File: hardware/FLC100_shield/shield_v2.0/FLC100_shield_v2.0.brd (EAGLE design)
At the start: 99.1 x 78.7 mm, 68 parts, among them IC1 TSR 1-2450, IC4 MCP1640, J1 RJ11-6PTH, Q1 2N7000, Q2 2N7000, Q3 2N7000, Q4 2N7000, Q5 2N7000, Q6 2N7000, Q7 2N7000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

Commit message: Minor routing changes.
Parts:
- JP9: value CLOUD PWR -> CLOUD CTRL
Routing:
- net 6: track 38.6 -> 40.1 mm
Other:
- board text added: "Add diodes to select highest voltage between IOREF and +5V"
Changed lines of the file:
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@@
 <text x="-10.16" y="40.64" size="1.27" layer="26" ratio="10" rot="MR90">&gt;DRAWING_NAME</text>
 <text x="-5.08" y="38.1" size="1.27" layer="26" ratio="10" rot="MR90">&gt;PLOT_DATE_TIME</text>
-<text x="96.52" y="15.24" size="1.9304" layer="26" ratio="12" rot="MR0">FLC100 shield v1.0</text>
-<text x="96.52" y="17.78" size="1.016" layer="26" ratio="10" rot="MR0">http://github.com/stevemarple/FLC100_shield</text>
+<text x="96.52" y="15.24" size="1.9304" layer="122" ratio="12" rot="MR0">FLC100 shield v1.0</text>
+<text x="96.52" y="17.78" size="1.016" layer="122" ratio="10" rot="MR0">http://github.com/stevemarple/FLC100_shield</text>
 <wire x1="99.06" y1="77.47" x2="97.79" y2="78.74" width="0" layer="20" curve="90"/>
 <wire x1="1.27" y1="78.74" x2="0" y2="77.47" width="0" layer="20" curve="90"/>
@@
 <text x="1.27" y="75.565" size="1.27" layer="27" ratio="10">+3V3</text>
 <text x="14.605" y="76.835" size="1.016" layer="27" ratio="10">VIN</text>
-<text x="72.39" y="47.625" size="1.4224" layer="121" ratio="12" rot="R90">FLC100 shield v1.0</text>
+<text x="91.694" y="49.53" size="1.4224" layer="121" ratio="12" rot="R90">FLC100 shield v1.0</text>
 <wire x1="69.215" y1="10.795" x2="60.96" y2="10.795" width="0.254" layer="121"/>
 <wire x1="60.96" y1="10.795" x2="59.69" y2="9.525" width="0.254" layer="121"/>
@@
 <wire x1="60.325" y1="9.779" x2="59.69" y2="9.525" width="0.254" layer="121"/>
 <wire x1="53.34" y1="25.4" x2="99.06" y2="25.4" width="0.254" layer="122" style="longdash"/>
+<text x="32.385" y="40.005" size="1.524" layer="121" ratio="12">FLC100 shield v1.0</text>
+<text x="74.93" y="13.97" size="1.524" layer="121" ratio="12">FLC100 shield v1.0</text>
+<text x="-7.62" y="16.51" size="1.778" layer="122">Add diodes to select highest voltage
+between IOREF and +5V</text>
 </plain>
 <attributes>
@@
 <attribute name="VALUE" x="11.43" y="38.735" size="1.016" layer="27" ratio="10"/>
 </element>
-<element name="JP9" library="SparkFun" package="1X02" value="CLOUD PWR" x="83.82" y="33.02" smashed="yes">
-<attribute name="NAME" x="82.4738" y="34.8488" size="1.27" layer="25" ratio="10"/>
-<attribute name="VALUE" x="82.55" y="29.845" size="1.27" layer="27" ratio="10"/>
+<element name="JP9" library="SparkFun" package="1X02" value="CLOUD CTRL" x="83.82" y="33.02" smashed="yes">
+<attribute name="NAME" x="89.6112" y="30.4038" size="1.27" layer="25" ratio="10" rot="R90"/>
+<attribute name="VALUE" x="91.44" y="30.48" size="1.27" layer="27" ratio="10" rot="R90"/>
 </element>
 <element name="JP11" library="pinhead" package="2X03" value="ALT ISP" x="31.75" y="71.12" smashed="yes" rot="R180">
@@
 </element>
 <element name="XRF" library="SteveMarple" package="XBEE" value="" x="74.295" y="13.335" smashed="yes" rot="R270">
-<attribute name="NAME" x="97.79" y="11.43" size="1.27" layer="25" ratio="10" rot="R90"/>
+<attribute name="NAME" x="90.17" y="20.955" size="1.27" layer="25" ratio="10"/>
 <attribute name="VALUE" x="75.565" y="22.225" size="0.4064" layer="27" rot="R270"/>
 </element>
@@
 <element name="C2" library="SparkFun" package="CPOL-RADIAL-10UF-25V" value="4u7 25V" x="45.72" y="36.83" smashed="yes" rot="R270">
 <attribute name="NAME" x="48.26" y="32.385" size="1.27" layer="25" ratio="10" rot="R90"/>
-<attribute name="VALUE" x="49.911" y="32.385" size="1.27" layer="27" ratio="10" rot="R90"/>
+<attribute name="VALUE" x="49.911" y="31.115" size="1.27" layer="27" ratio="10" rot="R90"/>
 </element>
 <element name="U$5" library="SteveMarple" package="PAD" value="PAD" x="91.44" y="43.18" smashed="yes"/>
@@
 <wire x1="51.308" y1="73.152" x2="48.26" y2="76.2" width="0.254" layer="16"/>
 <wire x1="72.898" y1="73.152" x2="51.308" y2="73.152" width="0.254" layer="16"/>
-<wire x1="73.66" y1="63.5" x2="73.66" y2="72.39" width="0.254" layer="16"/>
-<wire x1="73.66" y1="72.39" x2="72.898" y2="73.152" width="0.254" layer="16"/>
-<wire x1="75.565" y1="61.595" x2="73.66" y2="63.5" width="0.254" layer="16"/>
+<wire x1="77.47" y1="63.5" x2="77.47" y2="68.58" width="0.254" layer="16"/>
+<wire x1="77.47" y1="68.58" x2="72.898" y2="73.152" width="0.254" layer="16"/>
+<wire x1="75.565" y1="61.595" x2="77.47" y2="63.5" width="0.254" layer="16"/>
 </signal>
 <signal name="XRF_HEARTBEAT">
@@
 </board>
 </drawing>
+<compatibility>
+<note version="6.3" minversion="6.2.2" severity="warning">
+Since Version 6.2.2 text objects can contain more than one line,
+which will not be processed correctly with this version.
+</note>
+</compatibility>
 </eagle>

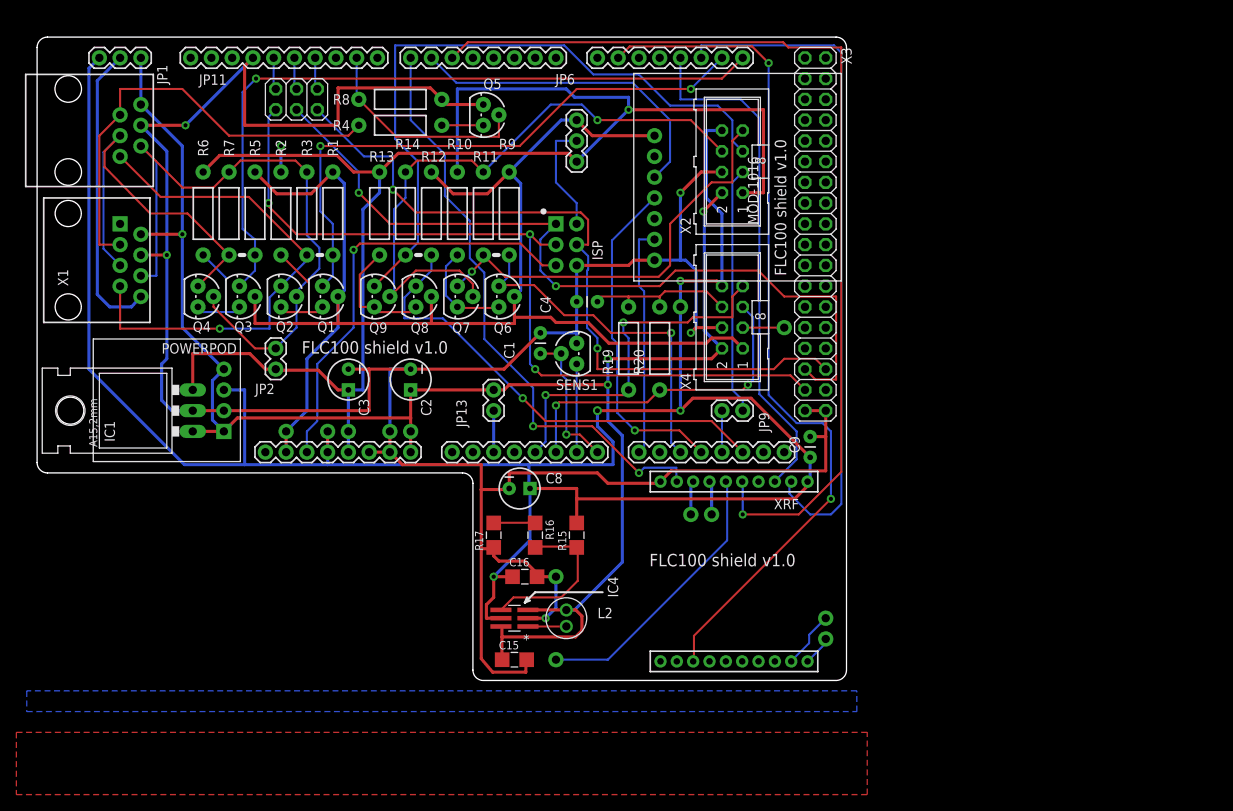
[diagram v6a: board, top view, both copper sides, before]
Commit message: Providing options for cloud detector level shifting pull-up voltage.
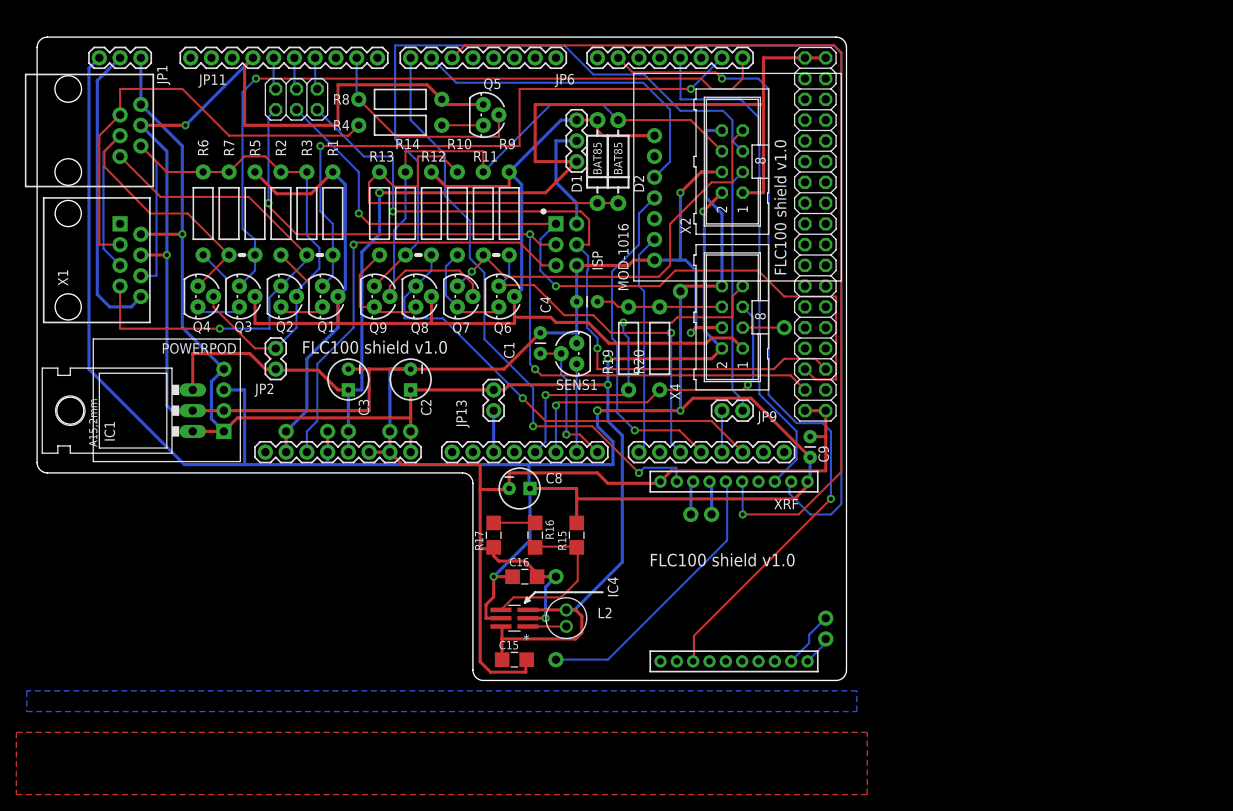
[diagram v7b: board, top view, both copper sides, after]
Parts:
- added D1, D2: BAT85, SteveMarple:DIODE-TH-0.4
- moved U$22 1.91 mm to (78.7, 47.6)
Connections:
- new net CLOUD_PULLUP: D1.C, D2.C, R10.P$2, R13.P$2
- net +5V: now also X3.1, X3.2; no longer R10.P$2, R13.P$2, R2.P$2, R6.P$2
- net CLOUD_VCC: now also D2.A
- net IOREF: now also D1.A
- net MAG_VCC: now also R2.P$2, R6.P$2
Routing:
- net CLOUD_PULLUP: track 0.00 -> 49.5 mm
- net +5V: track 186.6 -> 152.0 mm, vias 2 -> 1
- net CLOUD_VCC: track 75.4 -> 80.1 mm, vias 1 -> 0
- net SDA: track 71.9 -> 76.0 mm
- net N$22: track 19.5 -> 15.5 mm
- net XRF_ON: track 105.1 -> 102.1 mm
- net SCL: track 88.2 -> 90.7 mm
- net MOSI: track 90.9 -> 92.8 mm
- net MISO: track 99.1 -> 100.6 mm
- net IOREF: track 173.6 -> 174.9 mm
- net +3V3: track 271.0 -> 269.8 mm, vias 4 -> 3
- net MAG_VCC: track 78.4 -> 77.2 mm
- net 14: track 28.5 -> 27.4 mm
- net 6: track 40.1 -> 40.9 mm
- net !XRF_RESET: track 118.9 -> 118.2 mm

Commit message: Adding vias to improve ground pour.
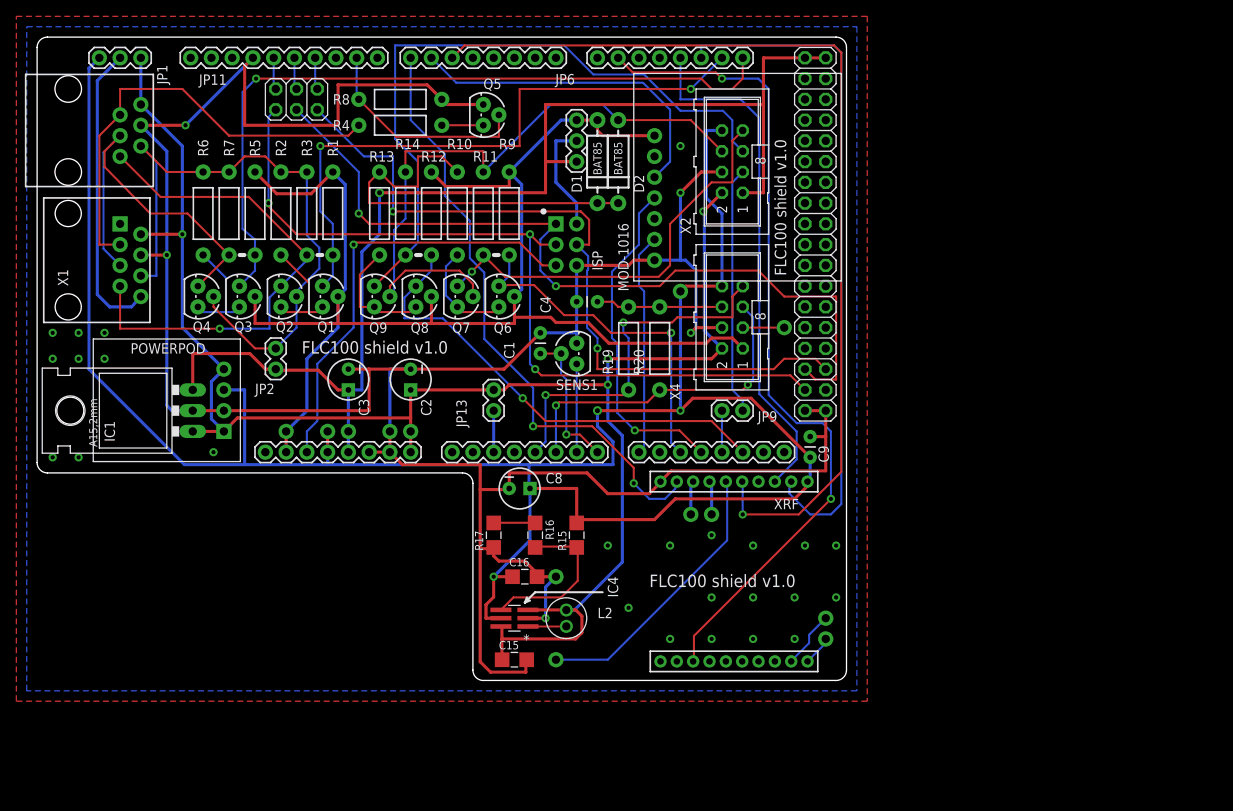
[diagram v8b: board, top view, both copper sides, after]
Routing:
- net +5V: track 152.0 -> 147.9 mm
- net XRF_SLEEP: track 73.2 -> 74.9 mm
- net GND: track 346.4 -> 347.5 mm, vias 5 -> 30
- net +3V3: track 269.8 -> 270.8 mm
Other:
- board text removed: "Add diodes to select highest voltage between IOREF and +5V"
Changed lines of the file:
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@@
 <wire x1="53.34" y1="24.13" x2="53.34" y2="1.27" width="0" layer="20"/>
 <text x="69.215" y="50.165" size="1.27" layer="25" ratio="10" rot="R90">ISP</text>
-<text x="-10.16" y="40.64" size="1.27" layer="26" ratio="10" rot="MR90">&gt;DRAWING_NAME</text>
-<text x="-5.08" y="38.1" size="1.27" layer="26" ratio="10" rot="MR90">&gt;PLOT_DATE_TIME</text>
-<text x="96.52" y="15.24" size="1.9304" layer="122" ratio="12" rot="MR0">FLC100 shield v1.0</text>
-<text x="96.52" y="17.78" size="1.016" layer="122" ratio="10" rot="MR0">http://github.com/stevemarple/FLC100_shield</text>
+<text x="16.51" y="36.83" size="1.016" layer="26" ratio="10" rot="MR0">&gt;DRAWING_NAME</text>
+<text x="16.51" y="34.925" size="1.016" layer="26" ratio="10" rot="MR0">&gt;PLOT_DATE_TIME</text>
+<text x="96.52" y="11.43" size="1.9304" layer="122" ratio="12" rot="MR0">FLC100 shield v1.0</text>
+<text x="96.52" y="13.97" size="1.016" layer="122" ratio="10" rot="MR0">http://github.com/stevemarple/FLC100_shield</text>
 <wire x1="99.06" y1="77.47" x2="97.79" y2="78.74" width="0" layer="20" curve="90"/>
 <wire x1="1.27" y1="78.74" x2="0" y2="77.47" width="0" layer="20" curve="90"/>
@@
 <wire x1="53.34" y1="25.4" x2="99.06" y2="25.4" width="0.254" layer="122" style="longdash"/>
 <text x="32.385" y="40.005" size="1.524" layer="121" ratio="12">FLC100 shield v1.0</text>
-<text x="74.93" y="13.97" size="1.524" layer="121" ratio="12">FLC100 shield v1.0</text>
-<text x="-7.62" y="16.51" size="1.778" layer="122">Add diodes to select highest voltage
-between IOREF and +5V</text>
+<text x="74.93" y="11.43" size="1.524" layer="121" ratio="12">FLC100 shield v1.0</text>
 </plain>
 <attributes>
@@
 </element>
 <element name="POWERPOD" library="SteveMarple" package="CISECO_POWERPOD_NCP1402" value="NCP1402 3V3" x="15.875" y="34.29" smashed="yes" rot="R90">
-<attribute name="NAME" x="15.24" y="40.005" size="1.27" layer="25" ratio="10"/>
+<attribute name="NAME" x="11.43" y="40.005" size="1.27" layer="25" ratio="10"/>
 <attribute name="VALUE" x="11.43" y="38.735" size="1.016" layer="27" ratio="10"/>
 </element>
@@
 <wire x1="88.9" y1="59.69" x2="86.36" y2="59.69" width="0.381" layer="1"/>
 <wire x1="88.9" y1="70.485" x2="88.9" y2="59.69" width="0.381" layer="1"/>
-<wire x1="60.96" y1="70.485" x2="88.9" y2="70.485" width="0.381" layer="1"/>
-<wire x1="66.04" y1="63.5" x2="60.96" y2="63.5" width="0.381" layer="1"/>
-<wire x1="60.96" y1="63.5" x2="60.96" y2="70.485" width="0.381" layer="1"/>
+<wire x1="62.23" y1="70.485" x2="88.9" y2="70.485" width="0.381" layer="1"/>
+<wire x1="62.23" y1="63.5" x2="62.23" y2="70.485" width="0.381" layer="1"/>
 <wire x1="62.23" y1="59.69" x2="41.91" y2="59.69" width="0.381" layer="1"/>
-<wire x1="66.04" y1="63.5" x2="62.23" y2="59.69" width="0.381" layer="1"/>
+<wire x1="66.04" y1="63.5" x2="62.23" y2="63.5" width="0.381" layer="1"/>
+<wire x1="62.23" y1="63.5" x2="62.23" y2="59.69" width="0.381" layer="1"/>
 <wire x1="39.751" y1="35.56" x2="38.1" y2="35.56" width="0.381" layer="16"/>
 <wire x1="39.751" y1="52.451" x2="39.751" y2="35.56" width="0.381" layer="16"/>
@@
 <wire x1="54.9402" y1="7.62" x2="54.9402" y2="9.271" width="0.381" layer="1"/>
 <wire x1="56.769" y1="7.62" x2="54.9402" y2="7.62" width="0.381" layer="1"/>
-<wire x1="66.04" y1="23.495" x2="66.04" y2="22.225" width="0.381" layer="1"/>
+<wire x1="66.04" y1="23.495" x2="66.04" y2="19.685" width="0.381" layer="1"/>
 <wire x1="60.325" y1="23.495" x2="66.04" y2="23.495" width="0.381" layer="1"/>
 <wire x1="60.325" y1="17.145" x2="55.88" y2="12.7" width="0.381" layer="16"/>
@@
 <wire x1="92.71" y1="22.225" x2="94.234" y2="23.749" width="0.381" layer="1"/>
 <wire x1="94.234" y1="23.749" x2="94.234" y2="24.257" width="0.381" layer="1"/>
-<wire x1="66.04" y1="22.225" x2="92.71" y2="22.225" width="0.381" layer="1"/>
-<wire x1="66.04" y1="19.279" x2="66.04" y2="22.225" width="0.381" layer="1"/>
+<wire x1="66.04" y1="19.685" x2="75.565" y2="19.685" width="0.381" layer="1"/>
+<wire x1="75.565" y1="19.685" x2="78.105" y2="22.225" width="0.381" layer="1"/>
+<wire x1="78.105" y1="22.225" x2="92.71" y2="22.225" width="0.381" layer="1"/>
+<wire x1="66.04" y1="19.279" x2="66.04" y2="19.685" width="0.381" layer="1"/>
 <wire x1="94.234" y1="24.257" x2="94.295" y2="24.335" width="0.381" layer="1"/>
 <wire x1="78.74" y1="33.02" x2="78.74" y2="47.625" width="0.381" layer="16"/>
@@
 <polygon width="0.381" layer="16" isolate="0.6096">
 <vertex x="-1.27" y="-1.27"/>
-<vertex x="-1.27" y="-3.81"/>
-<vertex x="100.33" y="-3.81"/>
+<vertex x="-1.27" y="80.01"/>
+<vertex x="100.33" y="80.01"/>
 <vertex x="100.33" y="-1.27"/>
 </polygon>
@@
 <contactref element="C4" pad="2"/>
 <polygon width="0.381" layer="1" isolate="0.6096">
-<vertex x="-2.54" y="-6.35"/>
-<vertex x="-2.54" y="-13.97"/>
-<vertex x="101.6" y="-13.97"/>
-<vertex x="101.6" y="-6.35"/>
+<vertex x="-2.54" y="-2.54"/>
+<vertex x="-2.54" y="81.28"/>
+<vertex x="101.6" y="81.28"/>
+<vertex x="101.6" y="-2.54"/>
 </polygon>
 <wire x1="62.23" y1="7.62" x2="60.071" y2="7.62" width="0.381" layer="1"/>
@@
 <wire x1="96.52" y1="33.02" x2="93.98" y2="33.02" width="0.381" layer="1"/>
 <wire x1="76.327" y1="24.384" x2="76.295" y2="24.335" width="0.381" layer="1"/>
-<wire x1="68.58" y1="25.4" x2="69.85" y2="24.13" width="0.381" layer="1"/>
-<wire x1="69.85" y1="24.13" x2="76.2" y2="24.13" width="0.381" layer="1"/>
-<wire x1="57.785" y1="25.4" x2="68.58" y2="25.4" width="0.381" layer="1"/>
+<wire x1="67.31" y1="25.4" x2="69.85" y2="22.86" width="0.381" layer="1"/>
+<wire x1="69.85" y1="22.86" x2="74.93" y2="22.86" width="0.381" layer="1"/>
+<wire x1="74.93" y1="22.86" x2="76.2" y2="24.13" width="0.381" layer="1"/>
+<wire x1="57.785" y1="25.4" x2="67.31" y2="25.4" width="0.381" layer="1"/>
 <wire x1="57.785" y1="23.495" x2="57.785" y2="25.4" width="0.381" layer="1"/>
 <wire x1="76.2" y1="24.13" x2="76.295" y2="24.335" width="0.381" layer="1"/>
@@
 <wire x1="94.615" y1="29.845" x2="96.52" y2="29.845" width="0.381" layer="1"/>
 <wire x1="96.52" y1="29.845" x2="96.52" y2="33.02" width="0.381" layer="1"/>
+<via x="1.905" y="39.37" extent="1-16" drill="0.508"/>
+<via x="5.08" y="39.37" extent="1-16" drill="0.508"/>
+<via x="5.08" y="42.545" extent="1-16" drill="0.508"/>
+<via x="1.905" y="42.545" extent="1-16" drill="0.508"/>
+<via x="8.255" y="39.37" extent="1-16" drill="0.508"/>
+<via x="8.255" y="42.545" extent="1-16" drill="0.508"/>
+<via x="1.905" y="27.305" extent="1-16" drill="0.508"/>
+<via x="21.59" y="27.94" extent="1-16" drill="0.508"/>
+<via x="82.55" y="5.08" extent="1-16" drill="0.508"/>
+<via x="92.71" y="5.08" extent="1-16" drill="0.508"/>
+<via x="92.71" y="10.16" extent="1-16" drill="0.508"/>
+<via x="87.63" y="10.16" extent="1-16" drill="0.508"/>
+<via x="87.63" y="5.08" extent="1-16" drill="0.508"/>
+<via x="82.55" y="10.16" extent="1-16" drill="0.508"/>
+<via x="77.47" y="5.08" extent="1-16" drill="0.508"/>
+<via x="97.79" y="10.16" extent="1-16" drill="0.508"/>
+<via x="97.79" y="16.51" extent="1-16" drill="0.508"/>
+<via x="78.74" y="65.405" extent="1-16" drill="0.508"/>
+<via x="93.98" y="16.51" extent="1-16" drill="0.508"/>
+<via x="87.63" y="16.51" extent="1-16" drill="0.508"/>
+<via x="82.55" y="17.78" extent="1-16" drill="0.508"/>
+<via x="77.47" y="16.51" extent="1-16" drill="0.508"/>
+<via x="69.85" y="16.51" extent="1-16" drill="0.508"/>
+<via x="72.39" y="8.89" extent="1-16" drill="0.508"/>
+<via x="5.08" y="27.305" extent="1-16" drill="0.508"/>
 </signal>
 <signal name="VIN" class="1">
@@
 <contactref element="U$13" pad="7"/>
 <contactref element="XRF" pad="9"/>
-<wire x1="73.66" y1="25.4" x2="74.295" y2="26.035" width="0.254" layer="16"/>
-<wire x1="74.295" y1="26.035" x2="78.232" y2="26.035" width="0.254" layer="16"/>
-<wire x1="78.232" y1="26.035" x2="78.232" y2="24.384" width="0.254" layer="16"/>
-<wire x1="67.945" y1="31.115" x2="73.66" y2="25.4" width="0.254" layer="1"/>
+<wire x1="73.025" y1="24.13" x2="74.93" y2="22.225" width="0.254" layer="16"/>
+<wire x1="74.93" y1="22.225" x2="76.835" y2="22.225" width="0.254" layer="16"/>
+<wire x1="76.835" y1="22.225" x2="78.105" y2="23.495" width="0.254" layer="16"/>
+<wire x1="78.105" y1="23.495" x2="78.105" y2="24.13" width="0.254" layer="16"/>
+<wire x1="67.945" y1="31.115" x2="73.025" y2="26.035" width="0.254" layer="1"/>
+<wire x1="73.025" y1="26.035" x2="73.025" y2="24.13" width="0.254" layer="1"/>
 <wire x1="60.706" y1="31.115" x2="67.945" y2="31.115" width="0.254" layer="1"/>
 <wire x1="60.706" y1="35.814" x2="60.706" y2="31.115" width="0.254" layer="16"/>
@@
 <wire x1="45.72" y1="68.58" x2="49.911" y2="64.389" width="0.254" layer="16"/>
 <wire x1="45.72" y1="76.2" x2="45.72" y2="68.58" width="0.254" layer="16"/>
-<wire x1="78.232" y1="24.384" x2="78.295" y2="24.335" width="0.254" layer="16"/>
-<via x="73.66" y="25.4" extent="1-16" drill="0.508"/>
+<wire x1="78.105" y1="24.13" x2="78.295" y2="24.335" width="0.254" layer="16"/>
+<via x="73.025" y="24.13" extent="1-16" drill="0.508"/>
 <via x="60.706" y="31.115" extent="1-16" drill="0.508"/>
 </signal>
@@
 </board>
 </drawing>
-<compatibility>
-<note version="6.3" minversion="6.2.2" severity="warning">
-Since Version 6.2.2 text objects can contain more than one line,
-which will not be processed correctly with this version.
-</note>
-</compatibility>
 </eagle>
